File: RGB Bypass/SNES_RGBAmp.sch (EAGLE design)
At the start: 25 parts, among them U1 THS7374

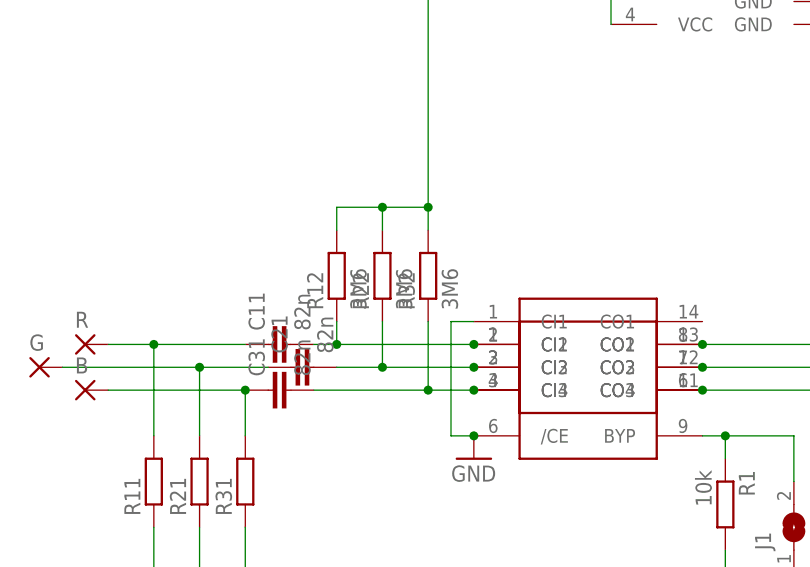
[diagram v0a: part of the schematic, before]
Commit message: Change resistor values
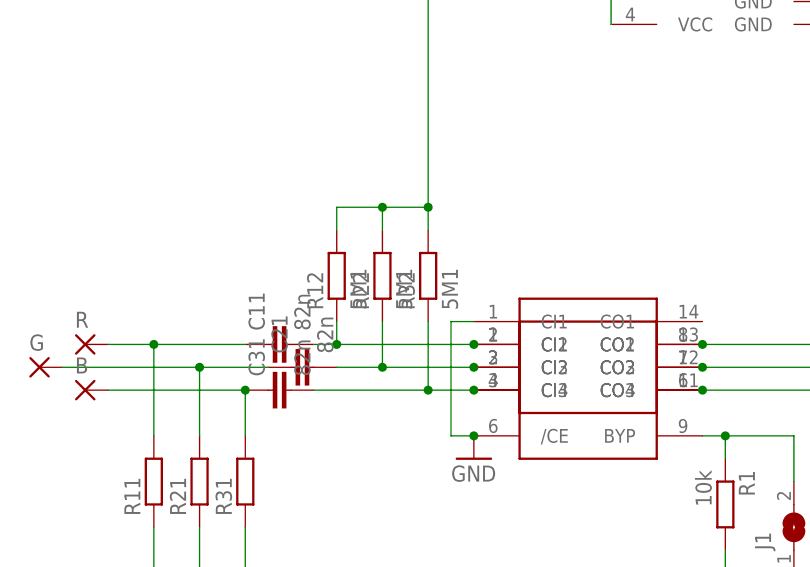
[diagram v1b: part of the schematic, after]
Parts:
- R12, R22, R32: value 3M6 -> 5M1
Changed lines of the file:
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@@
 <part name="R21" library="rcl" deviceset="R-EU_" device="R0603"/>
 <part name="R31" library="rcl" deviceset="R-EU_" device="R0603"/>
-<part name="R12" library="rcl" deviceset="R-EU_" device="R0603" value="3M6"/>
-<part name="R22" library="rcl" deviceset="R-EU_" device="R0603" value="3M6"/>
-<part name="R32" library="rcl" deviceset="R-EU_" device="R0603" value="3M6"/>
+<part name="R12" library="rcl" deviceset="R-EU_" device="R0603" value="5M1"/>
+<part name="R22" library="rcl" deviceset="R-EU_" device="R0603" value="5M1"/>
+<part name="R32" library="rcl" deviceset="R-EU_" device="R0603" value="5M1"/>
 <part name="R13" library="rcl" deviceset="R-EU_" device="R0603"/>
 <part name="R23" library="rcl" deviceset="R-EU_" device="R0603"/>
